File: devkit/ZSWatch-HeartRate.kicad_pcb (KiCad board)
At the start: 4 copper layers, 45 x 36.9 mm, 49 parts, among them IC101 MAX32664, IC102 MCP73832-2-OT, IC103 MAX86141, IC104 LIS2DS12, IC105 MIC5365-1.8, IC106 TPS61240, J101 I2C, J102 SPI, M101 BM15C, Q101 BSS138, SW101 RESET, SW102 BTN1, X101 CHARGE, X102 DEBUG, X103 BATTERY, Y101 32kHz

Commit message: Switch to new KiCad template, fixing CI/CD
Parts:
- LED101: value SFH 7016 -> SFH7016
- R101: footprint Capacitor_SMD:C_0603_1608Metric -> Resistor_SMD:R_0402_1005Metric
- moved R108 0.26 mm to (196.0, 145.9)
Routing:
- net Net-(M101-P2.03): track 41.7 -> 38.1 mm
- net GND: track 63.6 -> 62.9 mm, vias 33 -> 34

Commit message: doc: Update documentation
- Update README
- Update ref designators
- Update CI/CD pipeline

Signed-off-by: Daniel Kampert <DanielKampert@kampis-elektroecke.de>
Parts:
- D402: renamed from D102; value D_Photo -> VEMD8082
- D403: renamed from D103; value D_Photo -> VEMD8082
- renumbered C114 to C401, C115 to C402, C117 to C403, C118 to C404, C105 to C405, C101 to C406, C110 to C407, C103 to C408, C102 to C409, C104 to C410, C106 to C411, C107 to C412, C108 to C413, C109 to C414, C111 to C415, C112 to C416, C113 to C417, C116 to C418, D101 to D401, IC105 to IC401, IC106 to IC402, IC102 to IC403, IC101 to IC404, IC103 to IC405, IC104 to IC406, J101 to J401, J102 to J402, L101 to L401, LED101 to LED401, M101 to M401, Q101 to Q401, R101 to R401, R102 to R402, R103 to R403, R105 to R404, R106 to R405, R108 to R406, R109 to R407, R104 to R408, R107 to R409, R110 to R410, SW101 to SW401, SW102 to SW402, X101 to X401, X103 to X402, X102 to X403, Y101 to Y401

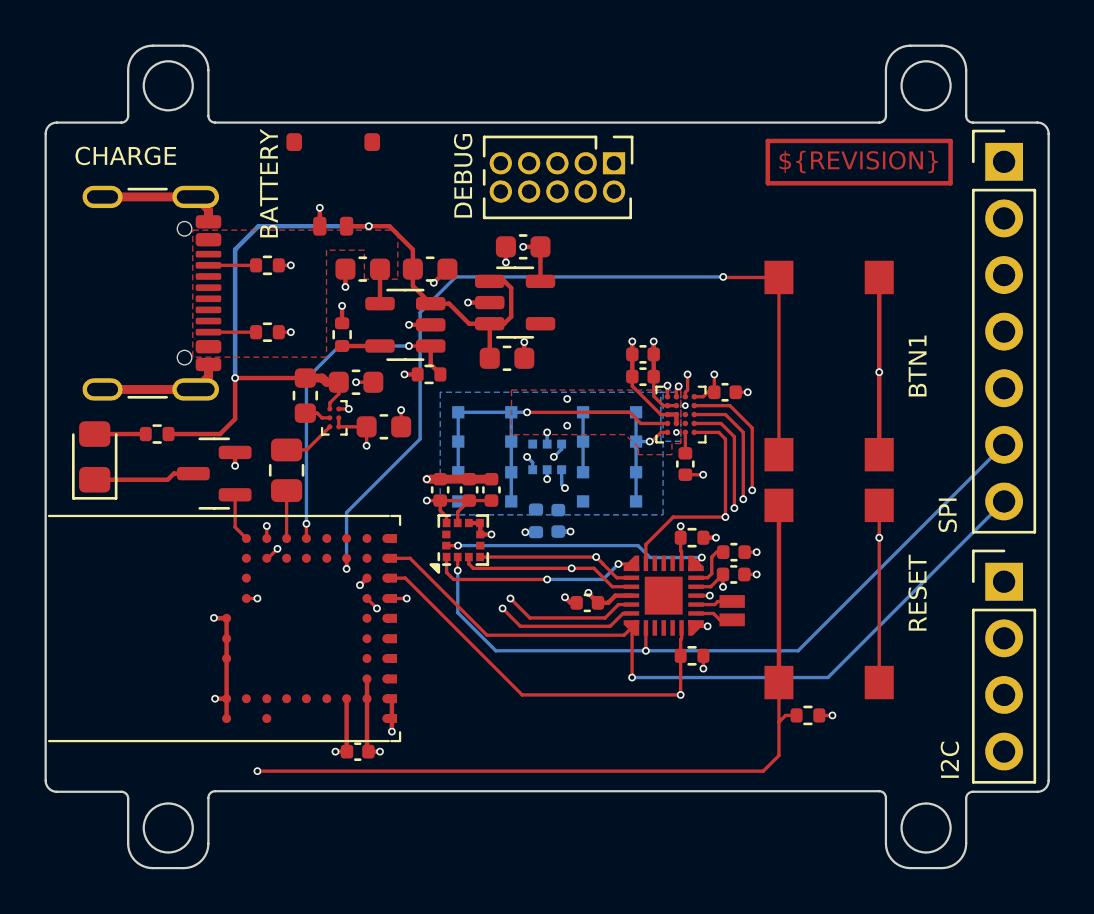
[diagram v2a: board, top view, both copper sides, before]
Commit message: Prepare release
- Set variant to CHECKED
- Remove unused files
- Fix ERC errors
- Fix DRC errors
- Fix different documentation errors
- Fix different path errors for the release build
- Remove Power Sequencing page
- Add PDF_REPORT_ROOT_DIR variable to build
- Add script for CHANGELOG generation

Signed-off-by: Daniel Kampert <DanielKampert@kampis-elektroecke.de>
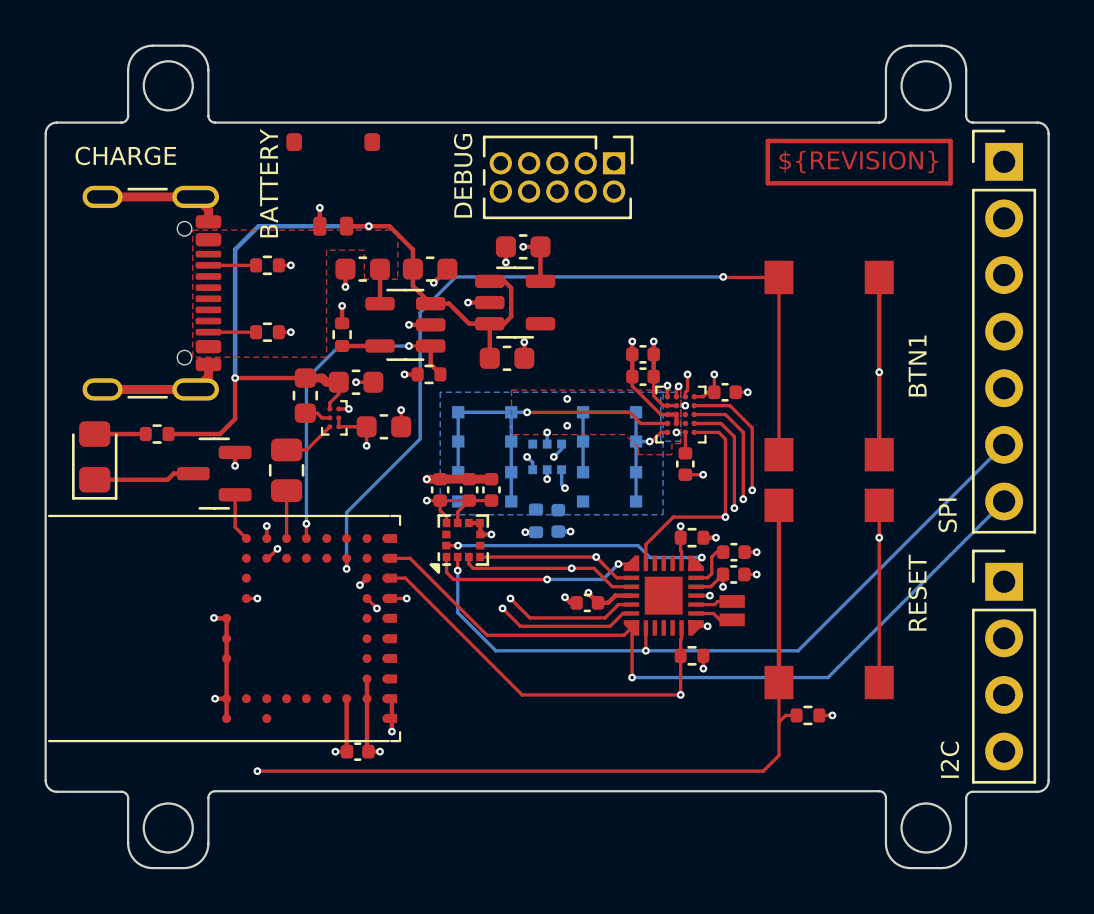
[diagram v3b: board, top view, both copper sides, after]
